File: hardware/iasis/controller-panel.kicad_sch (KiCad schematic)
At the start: 23 parts, among them SW1171 PTS645SL50SMTR92LFS, U1171 SN74AHCT1G125DBVR, U1172 TCA6408ARGTR

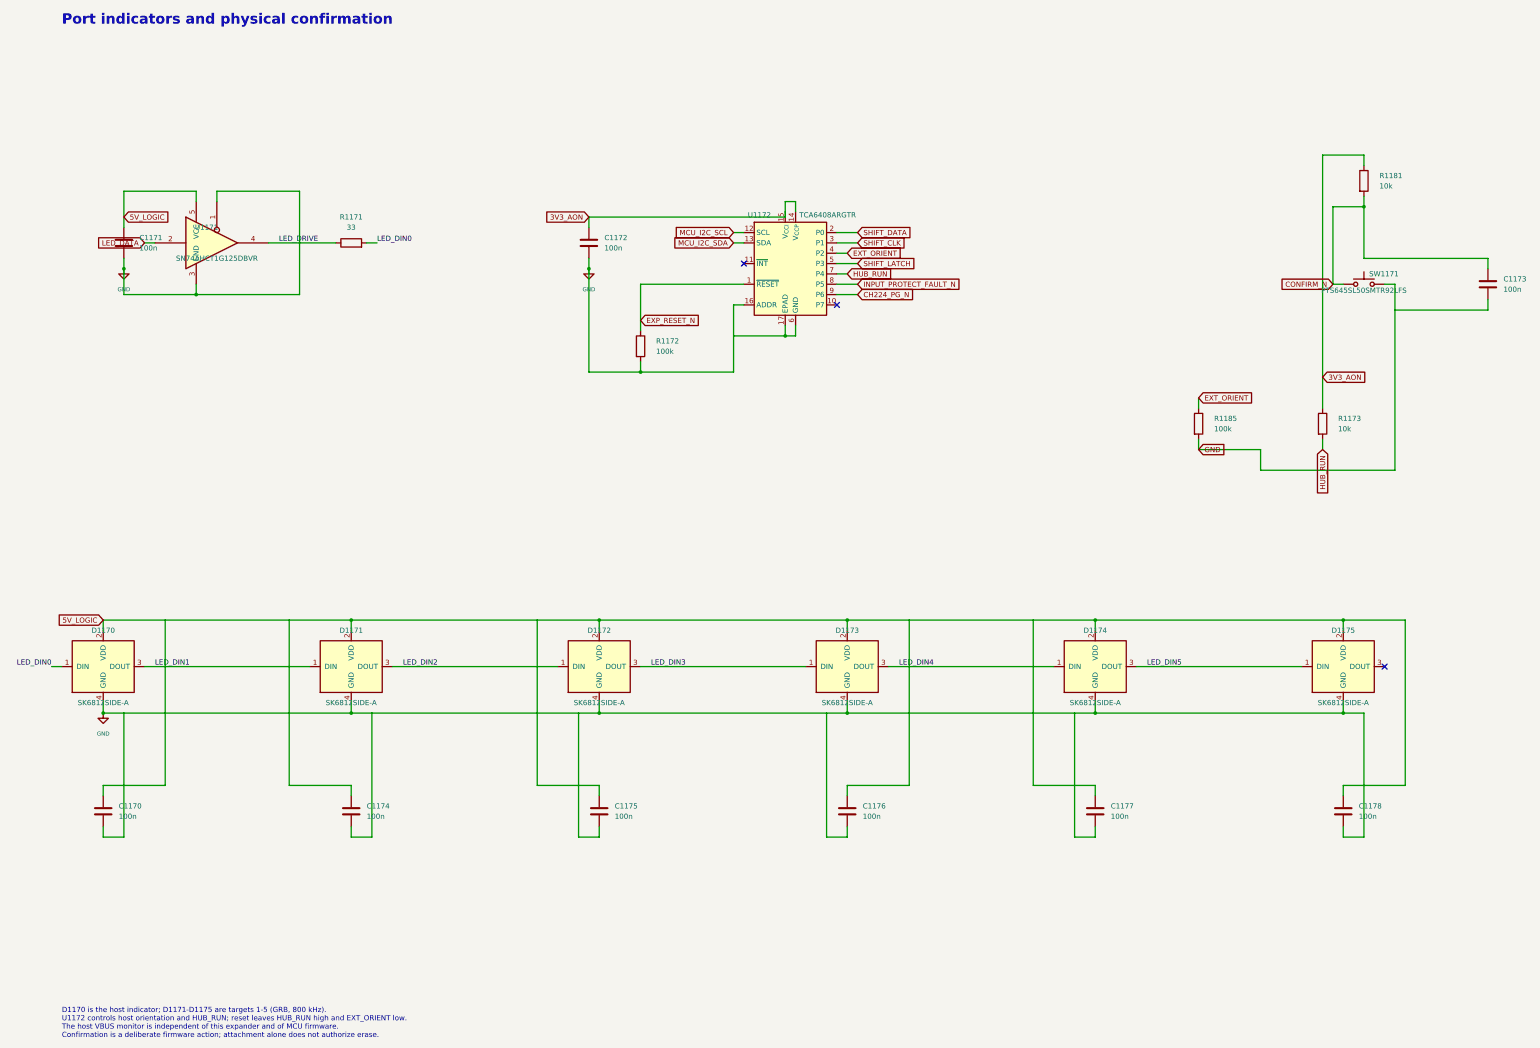
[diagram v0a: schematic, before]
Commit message: Add the CM5 carrier design for reference
The first board revision: a Raspberry Pi CM5 carrier with M.2 NVMe,
Ethernet and five USB 3 and USB-PD ports, as it stood before the compact
hub replaced it, squashed from 45 commits.
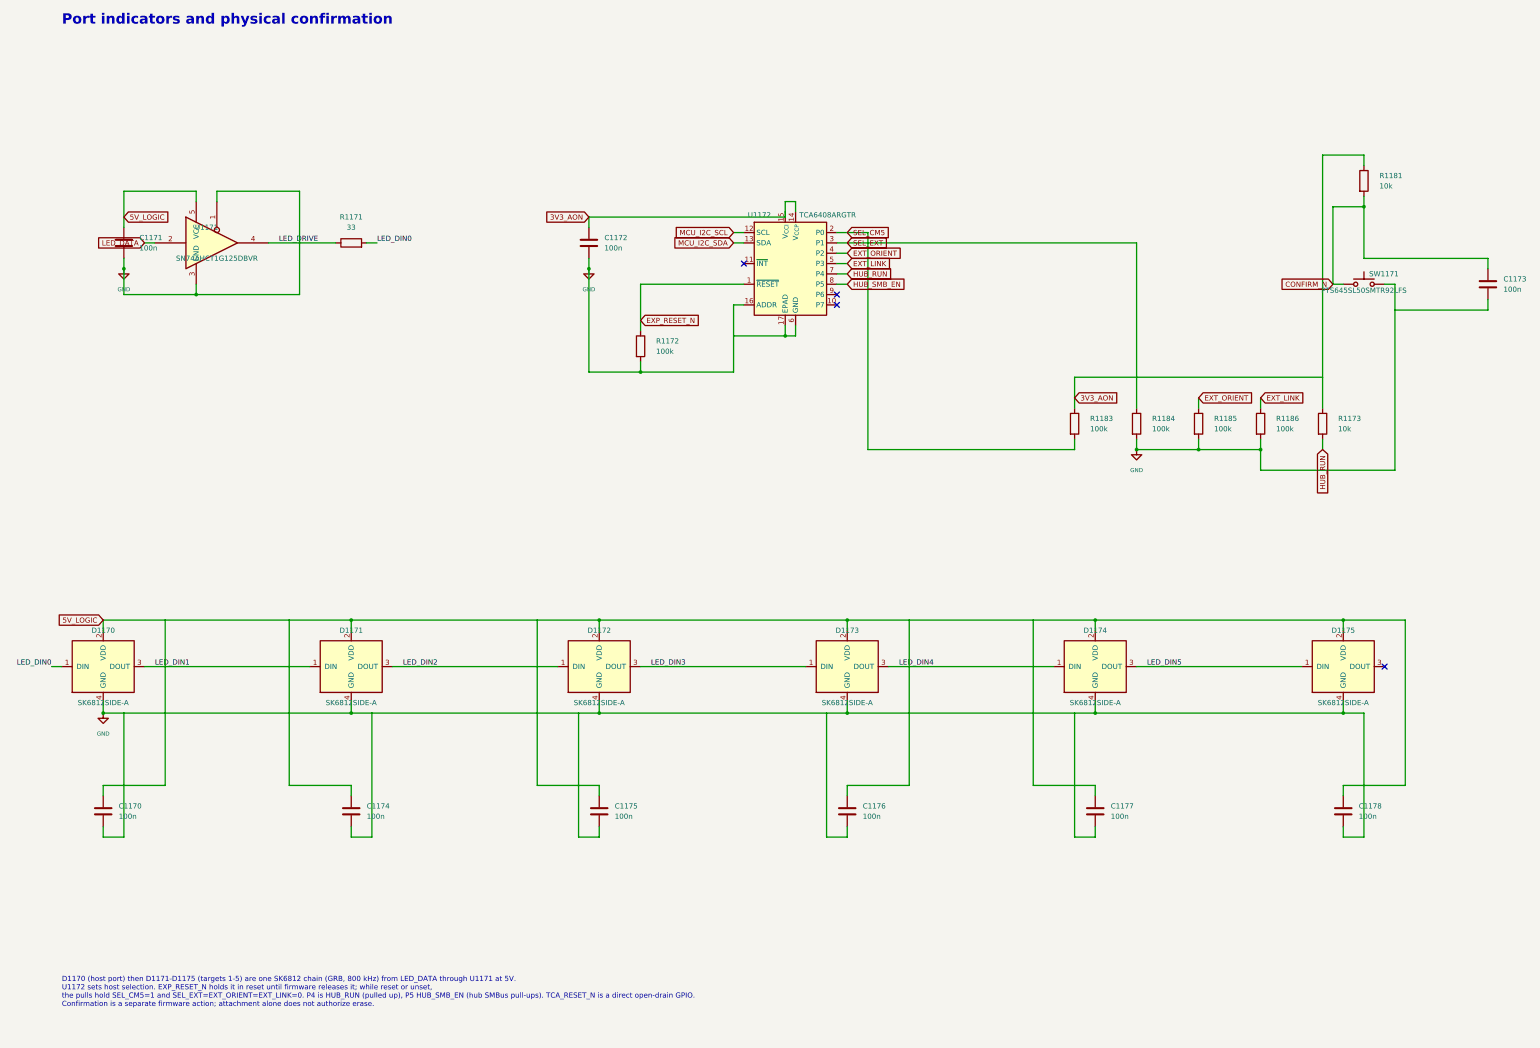
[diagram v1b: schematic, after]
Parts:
- added R1183, R1184, R1186: 100k, Resistor_SMD:R_0402_1005Metric, symbol Device:R
- C1170, C1171, C1172, C1173, C1174, C1175, C1176, C1177, C1178: LCSC C1525 -> (none); MPN CL05B104KO5NNNC -> (none); Manufacturer Samsung Electro-Mechanics -> (none)
- D1170, D1171, D1172, D1173, D1174, D1175: LCSC C5378721 -> (none); MPN SK6812SIDE-A -> (none); Manufacturer OPSCO Optoelectronics -> (none)
- R1171: LCSC C25105 -> (none); MPN 0402WGF330JTCE -> (none); Manufacturer UNI-ROYAL(Uniroyal Elec) -> (none)
- R1172, R1185: LCSC C25741 -> (none); MPN 0402WGF1003TCE -> (none); Manufacturer UNI-ROYAL(Uniroyal Elec) -> (none)
- R1173, R1181: LCSC C25744 -> (none); MPN 0402WGF1002TCE -> (none); Manufacturer UNI-ROYAL(Uniroyal Elec) -> (none)
- SW1171: LCSC C221877 -> (none); MPN PTS645SL50SMTR92LFS -> (none); Manufacturer C&K -> (none)
- U1171: LCSC C7484 -> (none); MPN SN74AHCT1G125DBVR -> (none); Manufacturer Texas Instruments -> (none)
- U1172: LCSC C181499 -> (none); MPN TCA6408ARGTR -> (none); Manufacturer Texas Instruments -> (none)
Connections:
- net 3V3_AON: now also R1183.1
- net GND: now also R1184.2, R1186.2
- net CH224_PG_N: no longer names the net of U1172.9 (P6)
- net INPUT_PROTECT_FAULT_N renamed HUB_SMB_EN
- net SHIFT_CLK renamed SEL_EXT
- net SEL_EXT: now also R1184.1
- net SHIFT_DATA renamed SEL_CM5
- net SEL_CM5: now also R1183.2
- net SHIFT_LATCH renamed EXT_LINK
- net EXT_LINK: now also R1186.1
- no-connect marks 3 -> 4
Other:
- note added: "D1170 (host port) then D1171-D1175 (targets 1-5) are one SK6812 chain (GRB, 800 kHz) from LED_DATA through U1171 at 5V. U1172 sets host selection. EXP_RESET_N holds it in reset until firmware releases it; while reset or unset, the pulls hold SEL_CM5=1 and SEL_EXT=EXT_ORIENT=EXT_LINK=0. P4 is HUB_RUN (pulled up), P5 HUB_SMB_EN (hub SMBus pull-ups). TCA_RESET_N is a direct open-drain GPIO. Confirma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"
- note removed: "D1170 is the host indicator; D1171-D1175 are targets 1-5 (GRB, 800 kHz). U1172 controls host orientation and HUB_RUN; reset leaves HUB_RUN high and EXT_ORIENT low. The host VBUS monitor is independent of this expander and of MCU firmware. Confirmation is a deliberate firmware action; attachment alone does not authorize erase."
